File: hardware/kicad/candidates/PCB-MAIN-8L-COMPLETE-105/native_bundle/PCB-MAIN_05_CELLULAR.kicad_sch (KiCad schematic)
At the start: 81 parts, among them J6 2336582-1, J7 2336582-1, J8 U.FL-R-SMT-1(60), Q1 MMBT3904,215, Q2 MMBT3904,215, Q3 MMBT3904,215, U13 TS3A27518EPWR, U14 ESDALC6V1-5P6, U15 ESDALC6V1-5P6, U16 SN74AXC8T245PWR, U26 2 channel 0.7 pF USB ESD, U27 4 channel 0.5 pF ESD, U8 BG95-M3

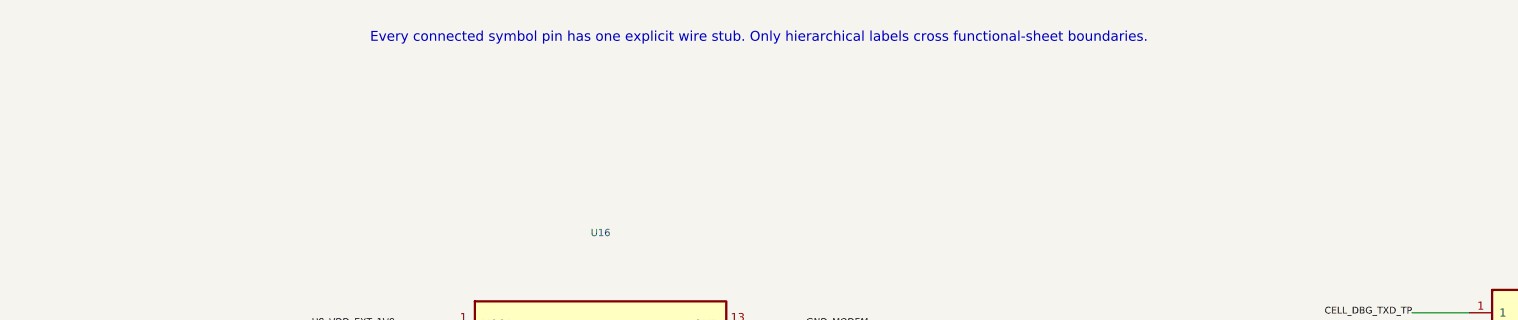
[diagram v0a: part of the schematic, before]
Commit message: PCB-MAIN Rev B: bilingual schematic notes and PDF
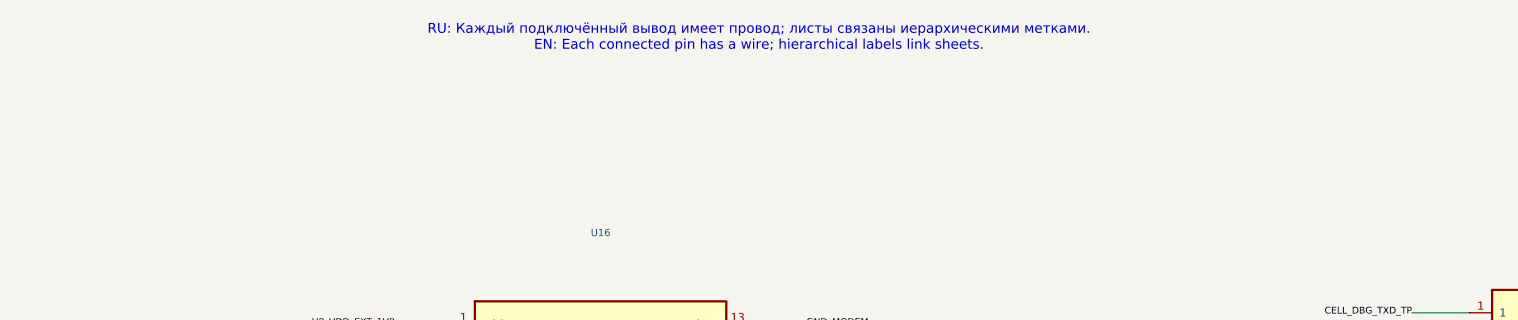
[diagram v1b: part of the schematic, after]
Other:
- note added: "RU: Каждый подключённый вывод имеет провод; листы связаны иерархическими метками. EN: Each connected pin has a wire; hierarchical labels link sheets."
- note removed: "Every connected symbol pin has one explicit wire stub. Only hierarchical labels cross functional-sheet boundaries."
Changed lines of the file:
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@@
     (stroke (width 0.0))
   )
-  (text "Every connected symbol pin has one explicit wire stub. Only hierarchical labels cross functional-sheet boundaries."
+  (text "RU: Каждый подключённый вывод имеет провод; листы связаны иерархическими метками.\nEN: Each connected pin has a wire; hierarchical labels link sheets."
     (at 297.0 12.7 0)
     (effects (font (size 1.1 1.1)))
